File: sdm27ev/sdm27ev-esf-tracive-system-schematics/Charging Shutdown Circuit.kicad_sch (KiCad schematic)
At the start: 10 parts, among them K11 1, K12 2, K5 AIR +, K6 AIR -, K7 Precharge, K9 Discharge

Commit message: Charging Shutdown Updated
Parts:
- removed BT17: 12 V Power, symbol Device:Battery
- removed F11: Fuse, symbol Device:Fuse
- removed K11: 1, symbol Relay:Relay_SPST-NO
- removed K5: AIR +, symbol Relay:Relay_SPST-NO
- removed K9: Discharge, symbol Relay:Relay_SPST-NC
- removed R5, R6: R_US, symbol Device:R_US
- added D2, D3: D, Diode_SMD:SODFL1608X70N, symbol Device:D
- added D5: BMS, LED_SMD:LED_0603_1608Metric, symbol Device:LED
- added D6: IMD, LED_SMD:LED_0603_1608Metric, symbol Device:LED
- added F12: 500A, symbol Device:Fuse
- added J2: TS_Container Interlock, symbol Connector_Generic:Conn_02x01_Row_Letter_First
- added J3: Energy Meter Interlock, symbol Connector_Generic:Conn_02x01_Row_Letter_First
- added J4: Precharge Control, symbol Connector_Generic:Conn_02x02_Counter_Clockwise
- added J5: Elcon Charger, symbol Connector_Generic:Conn_02x02_Counter_Clockwise
- added K11, K14: PR22-12V-400-1A, Misc_footprints:PR2212V4001A, symbol V23047A1012A511:PR22-12V-400-1A
- added K13: Discharge Relay, Relay_THT:Relay_SPST_StandexMeder_MS_Form1AB, symbol Relay:MSxx-1Bxx-75
- added K9: Isolation_Relay_+, symbol Relay:Relay_SPST-NO
- added Q2, Q3: ZXM61N02FTC, Misc_footprints:ZXM61N02FTC, symbol V23047A1012A511:ZXM61N02FTC
- added R10, R14: 680, Resistor_SMD:R_0603_1608Metric, symbol Device:R
- added R11: 600, symbol Device:R
- added R12: 2k, symbol Device:R
- added R13, R16: 10k, Resistor_SMD:R_0603_1608Metric, symbol Device:R
- added R15, R9: 10k, symbol Device:R
- added SW5: Charging_Shutdown_Button, symbol Switch:SW_SPST
- added TP1: TSMP+, symbol Connector:TestPoint
- added TP2: TSMP-, symbol Connector:TestPoint
- added TS_Battery1: Battery, symbol Device:Battery
- K12: value 2 -> Isolation Relay -
- K6: value AIR - -> Main Contactor Relay
- K7: value Precharge -> Precharge Relay
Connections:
- net at K7.14: now also K6.13, K9.13
- net at K6.A1: now also J4.4 (Pin_4), K9.A2; no longer K7.A1
- net HV-: now reaches K12.13
- net HV-: now also K12.14, K13.7, R15.1, TS_Battery1.2 (-)
- net at K12.A1: now also K7.A2, J4.3 (Pin_3)
- net GND: now reaches K12.A2
- net GND: now also K6.A2, K7.A1, D2.2 (A), D3.2 (A), J4.2 (Pin_2), J5.3 (Pin_3), K13.3, K9.A1, Q2.3 (S), Q3.3 (S), R13.1, R16.1
- net HV+: now reaches K6.14
- net HV+: now also F12.2, R11.1, R12.1, R9.2, TS_Battery1.1 (+)
- net at K7.13: now also R11.2
- new net: D5.2 (A), R10.1
- new net: K11.6 (COIL_2), R10.2
- new net: J3.b1 (Pin_b1), J4.1 (Pin_1), K13.5
- new net: F12.1, K9.14
- new net: R9.1, TP1.1
- new net: D6.1 (K), Q3.2 (D)
- new net: J2.a1 (Pin_a1), J3.a1 (Pin_a1)
- new net: J2.b1 (Pin_b1), SW5.2 (B)
- new net: K13.1, R12.2
- new net: D6.2 (A), R14.1
- new net: K14.6 (COIL_2), R14.2
- new net: K11.3 (NO_1), K14.2 (COM_1)
- new net: K14.3 (NO_1), SW5.1 (A)
- new net: D5.1 (K), Q2.2 (D)
- new net: R15.2, TP2.1
- new net +12V: D2.1 (K), D3.1 (K), J5.4 (Pin_4), K11.1 (COIL_1), K11.2 (COM_1), K14.1 (COIL_1)
- new net BMS KILL SIGNAL: Q2.1 (G), R13.2
- new net CAN H: J5.1 (Pin_1)
- new net CAN L: J5.2 (Pin_2)
- new net IMD KILL SIGNAL: Q3.1 (G), R16.2
- no-connect marks 0 -> 4
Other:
- note added: "(TSMPs are physically same connector)"
- note added: "18 AWG"
- note added: "2 AWG"
- note added: "BMS and IMD separate circuits, input signals are latched externally"
- note added: "CAN going to BMS"
- note added: "Charger Box"
- note added: "Discharge"
- note added: "Precharge"
- note added: "TSMP +"
- note added: "TSMP -"
- note added: "Tractive Container"
- note removed: "12V"
- note removed: "AC Power"
- note removed: "ACCUMULATOR"
- note removed: "AIR IN"
- note removed: "AIR OUT"
- note removed: "All Unmarked Wiring is 18 AWG"
- note removed: "B+"
- note removed: "B-"
- note removed: "BSPD_Sensor"
- note removed: "Batteries"
- note removed: "CAN High"
- note removed: "CAN Low"
- note removed: "CHARGING CART"
- note removed: "Charging Shutdown Circuit"
- note removed: "ELCON HK-J-H650"
- note removed: "GND"
- note removed: "IMD"
- note removed: "Orion 2 BMS"
- note removed: "Precharge Control"
- note removed: "the charging shutdown needs to connect to the normal shutdowen to control IR's and a GLV relay to turn off the charger"

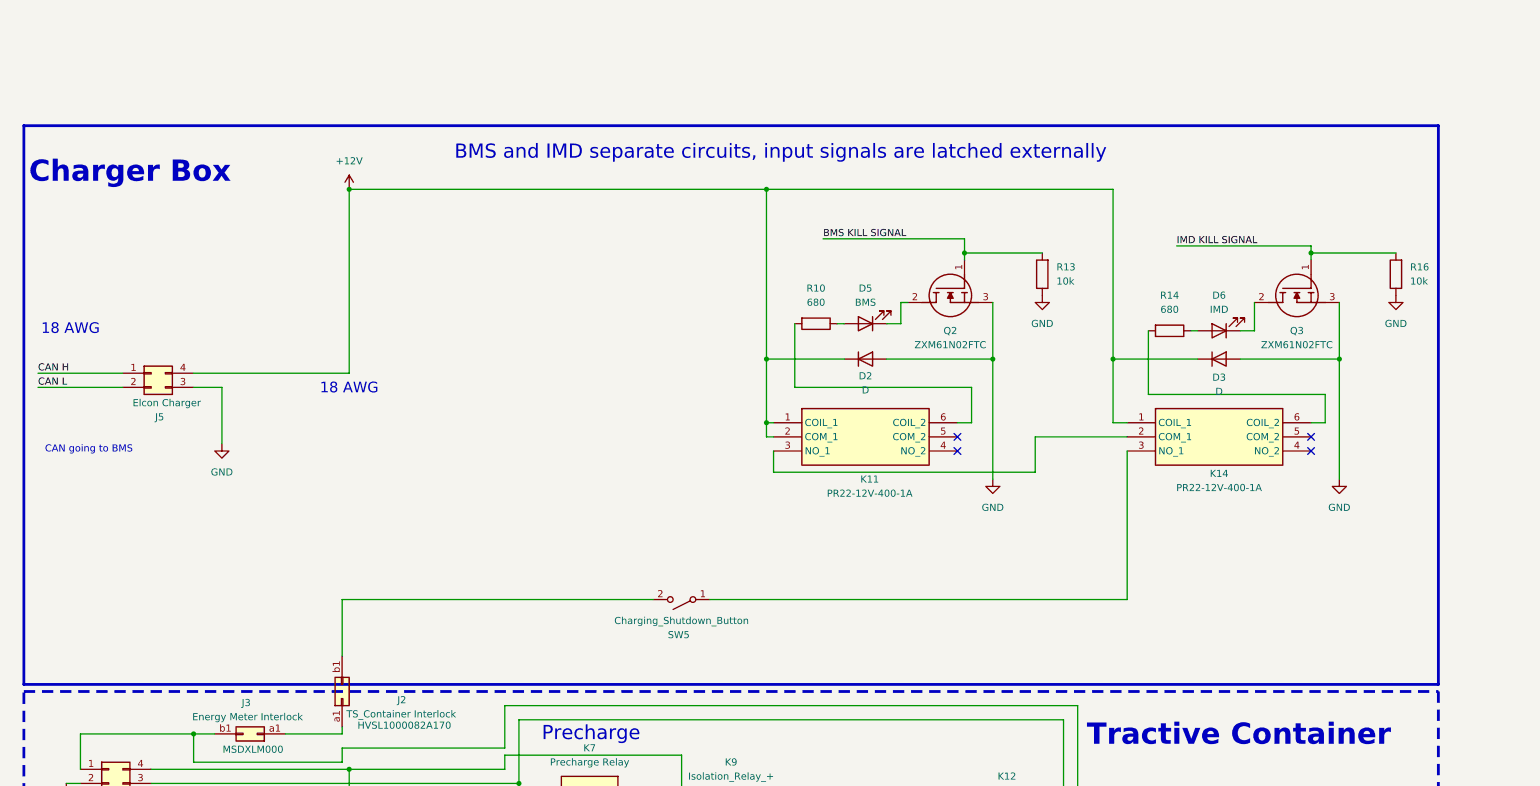
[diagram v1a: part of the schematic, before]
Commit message: Added/FIxed ESF connectors Tractive system & Charger
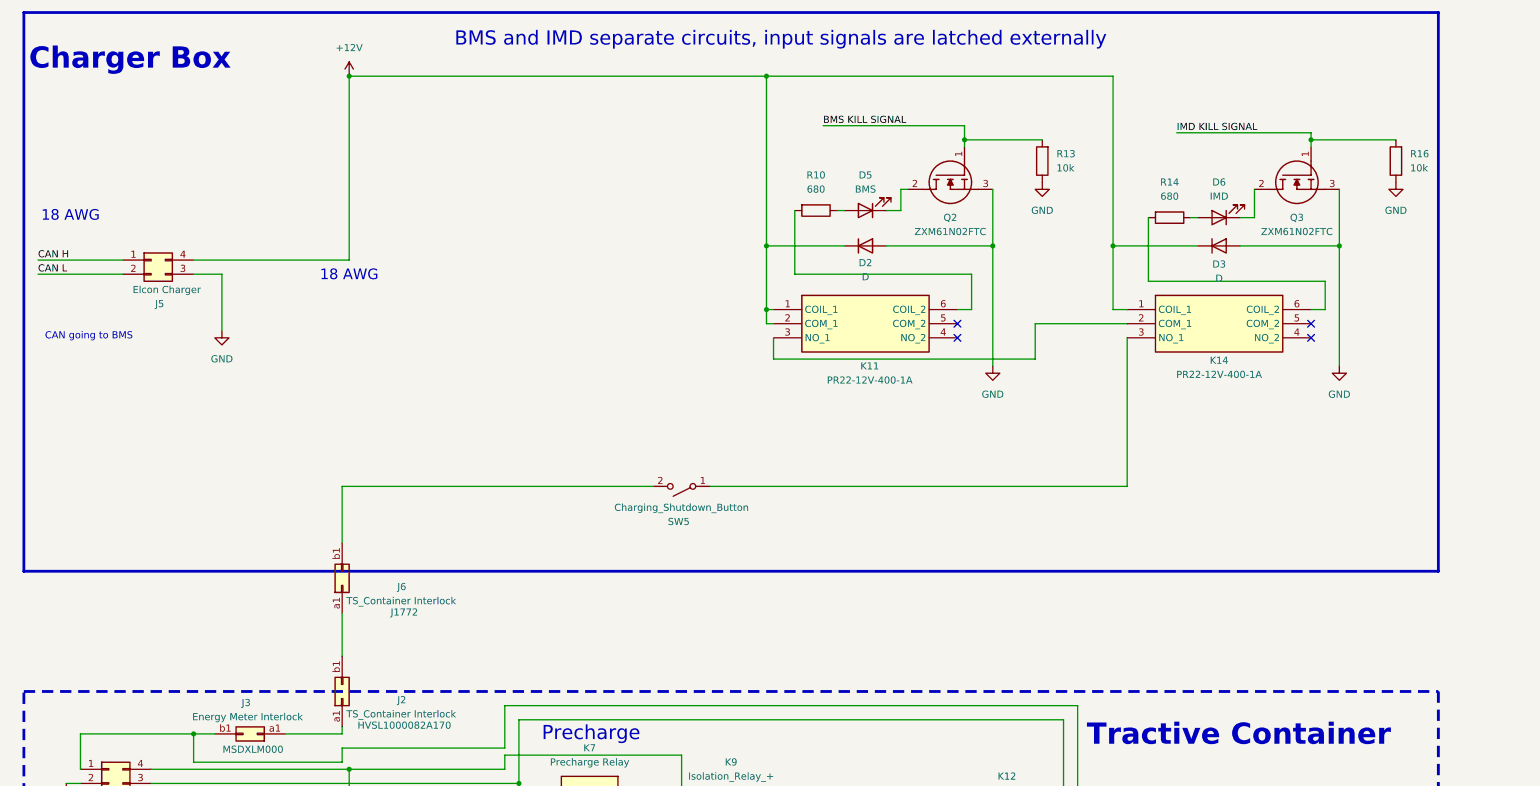
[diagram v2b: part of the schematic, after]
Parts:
- added J6: TS_Container Interlock, symbol Connector_Generic:Conn_02x01_Row_Letter_First
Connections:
- net at J2.b1 (Pin_b1): now also J6.a1 (Pin_a1); no longer SW5.2 (B)
- new net: J6.b1 (Pin_b1), SW5.2 (B)
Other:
- moved on the sheet: D2, D3, D5, D6, J5, K11, K14, Q2, Q3, R10, R13, R14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
